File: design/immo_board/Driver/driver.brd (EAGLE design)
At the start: 121.4 x 122.5 mm, 41 parts, among them IC1 7812TV, IC10 7805TV, IC2 LM393N, IC3 74LS241N, IC4 7812TV, IC5 7812TV, IC6 7812TV, IC7 7812TV, IC8 7805TV, IC9 7805TV

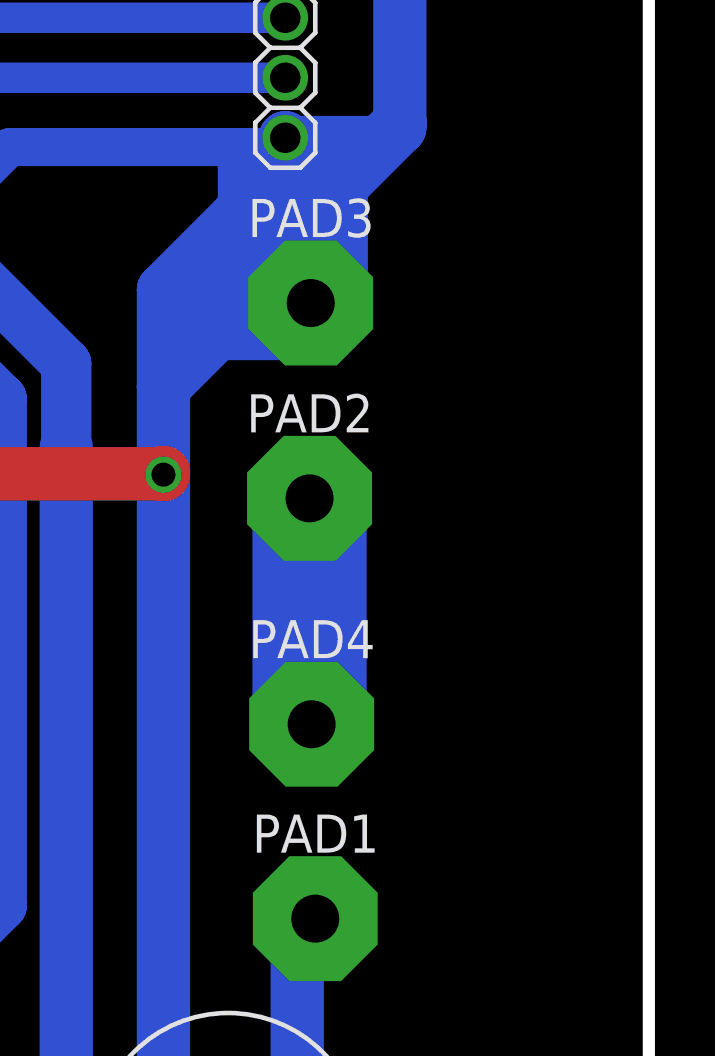
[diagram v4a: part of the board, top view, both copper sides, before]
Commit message: Fix driver scheme (supply switch)
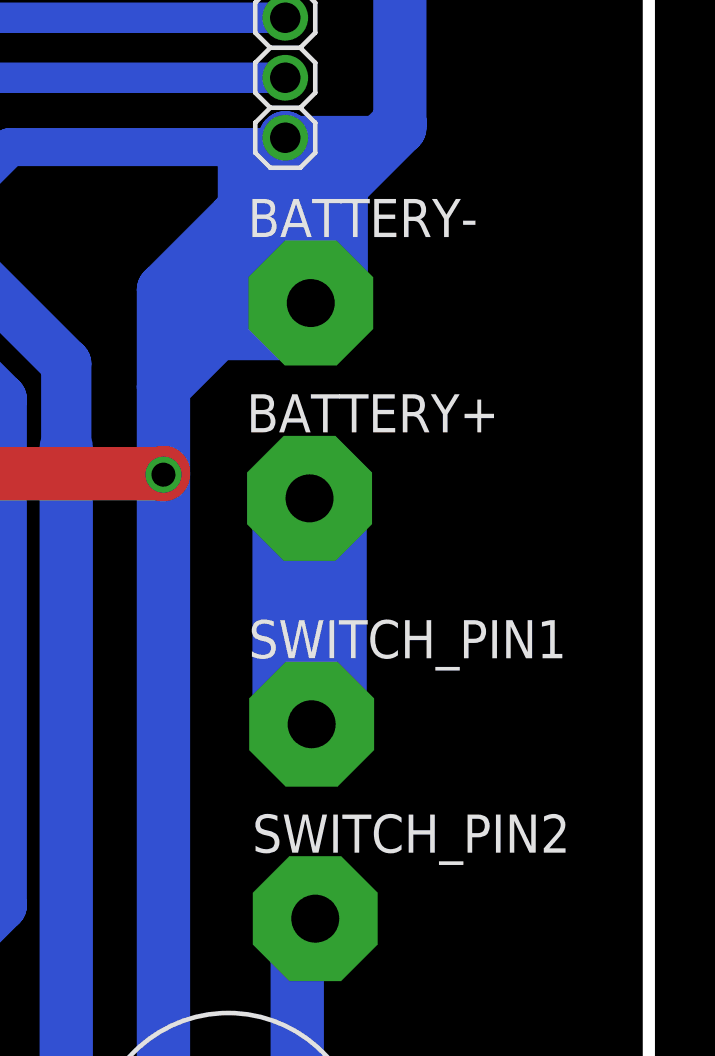
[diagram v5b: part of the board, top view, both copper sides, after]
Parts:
- renumbered PAD1 to SWITCH_PIN2, PAD2 to BATTERY+, PAD3 to BATTERY-, PAD4 to SWITCH_PIN1
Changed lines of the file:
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@@
 <attribute name="OC_NEWARK" value="unknown" x="62.32" y="93.47" size="1.778" layer="27" display="off"/>
 </element>
-<element name="PAD1" library="wirepad" package="4,16O1,6" value="WIREPAD4,16O1,6" x="151.03" y="13.48"/>
-<element name="PAD2" library="wirepad" package="4,16O1,6" value="WIREPAD4,16O1,6" x="150.84" y="27.49"/>
-<element name="PAD3" library="wirepad" package="4,16O1,6" value="WIREPAD4,16O1,6" x="150.88" y="34"/>
-<element name="PAD4" library="wirepad" package="4,16O1,6" value="WIREPAD4,16O1,6" x="150.91" y="19.96"/>
+<element name="SWITCH_PIN2" library="wirepad" package="4,16O1,6" value="WIREPAD4,16O1,6" x="151.03" y="13.48"/>
+<element name="BATTERY+" library="wirepad" package="4,16O1,6" value="WIREPAD4,16O1,6" x="150.84" y="27.49"/>
+<element name="BATTERY-" library="wirepad" package="4,16O1,6" value="WIREPAD4,16O1,6" x="150.88" y="34"/>
+<element name="SWITCH_PIN1" library="wirepad" package="4,16O1,6" value="WIREPAD4,16O1,6" x="150.91" y="19.96"/>
 <element name="C1" library="resistor" package="E5-8,5" value="" x="137.94" y="0.49"/>
 <element name="C2" library="resistor" package="E2,5-5" value="" x="137.91" y="0.43"/>
@@
 <wire x1="60.43" y1="40.1" x2="57.7" y2="40.1" width="1.778" layer="16"/>
 <wire x1="57.69" y1="40.09" x2="57.7" y2="40.1" width="1.778" layer="16"/>
-<contactref element="PAD3" pad="1"/>
+<contactref element="BATTERY-" pad="1"/>
 <wire x1="134.63" y1="51.22" x2="137.17" y2="51.22" width="1.6764" layer="16"/>
 <wire x1="130.72" y1="28.35" x2="137.12" y2="28.35" width="1.778" layer="16"/>
@@
 <wire x1="57.67" y1="57.53" x2="67.22" y2="57.53" width="1.778" layer="16"/>
 <wire x1="67.22" y1="57.53" x2="67.71" y2="57.04" width="1.778" layer="16"/>
-<contactref element="PAD1" pad="1"/>
+<contactref element="SWITCH_PIN2" pad="1"/>
 <contactref element="C5" pad="+"/>
 <contactref element="C6" pad="+"/>
@@
 </signal>
 <signal name="VCC">
-<contactref element="PAD2" pad="1"/>
+<contactref element="BATTERY+" pad="1"/>
 <wire x1="150.84" y1="27.49" x2="150.84" y2="20.03" width="3.81" layer="16"/>
-<contactref element="PAD4" pad="1"/>
+<contactref element="SWITCH_PIN1" pad="1"/>
 <wire x1="150.91" y1="19.96" x2="150.84" y2="20.03" width="0" layer="19" extent="16-16"/>
 </signal>
